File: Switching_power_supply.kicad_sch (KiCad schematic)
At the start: 32 parts, among them J8 Conn_01x03_Pin, SW1 SW_DIP_x04, U4 AMS1117, U5 LM2596HVS-ADJRG

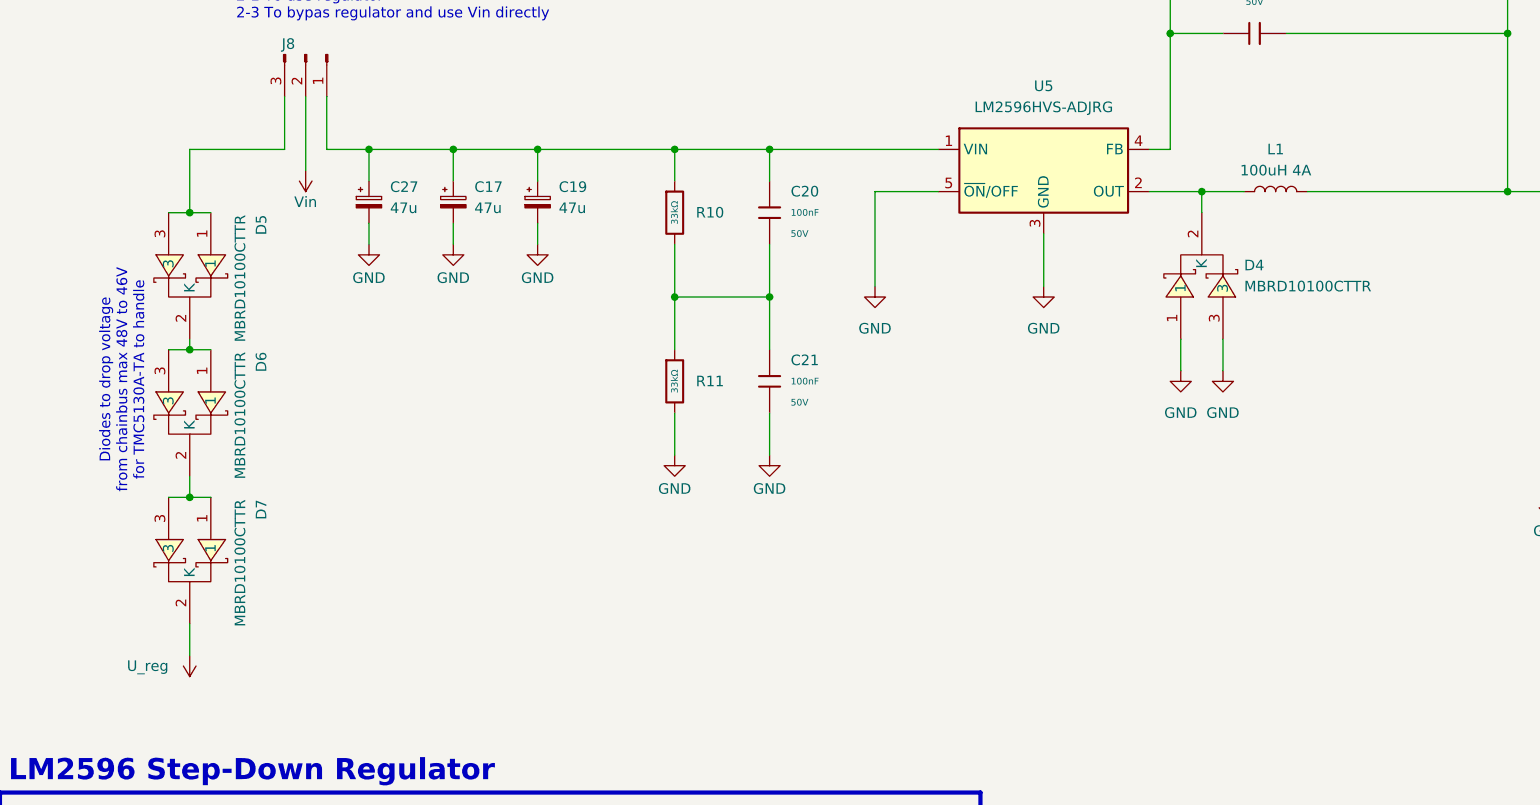
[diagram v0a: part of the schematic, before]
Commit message: added clearance for mounting
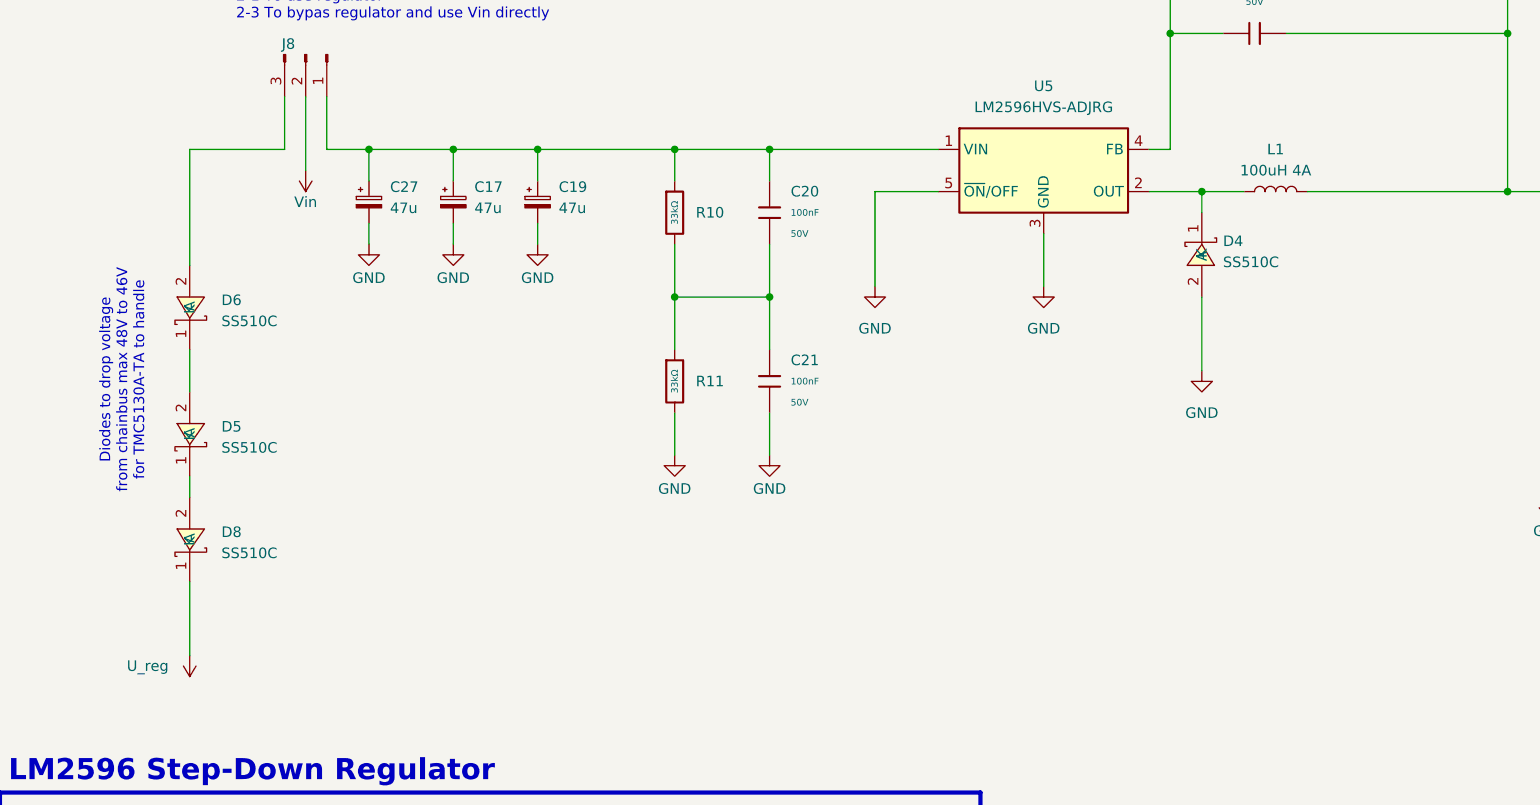
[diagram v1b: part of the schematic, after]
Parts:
- removed D4, D5, D6, D7: MBRD10100CTTR, SMC_MBRD10100CTTR:TO-252-3_L6.5-W5.8-P4.58-TL, symbol SMC_MBRD10100CTTR:MBRD10100CTTR
- added D4, D5, D6, D8: SS510C, SS510C:SMC_L7.1-W6.2-LS8.1-RD, symbol SS510C:SS510C
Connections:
- net GND: now also D4.2 (A)
- net U_reg: now also D8.1 (K)
- net at L1.1, U5.2 (OUT): now also D4.1 (K)
- net at J8.3 (Pin_3): now also D6.2 (A)
- new net: D5.2 (A), D6.1 (K)
- new net: D5.1 (K), D8.2 (A)

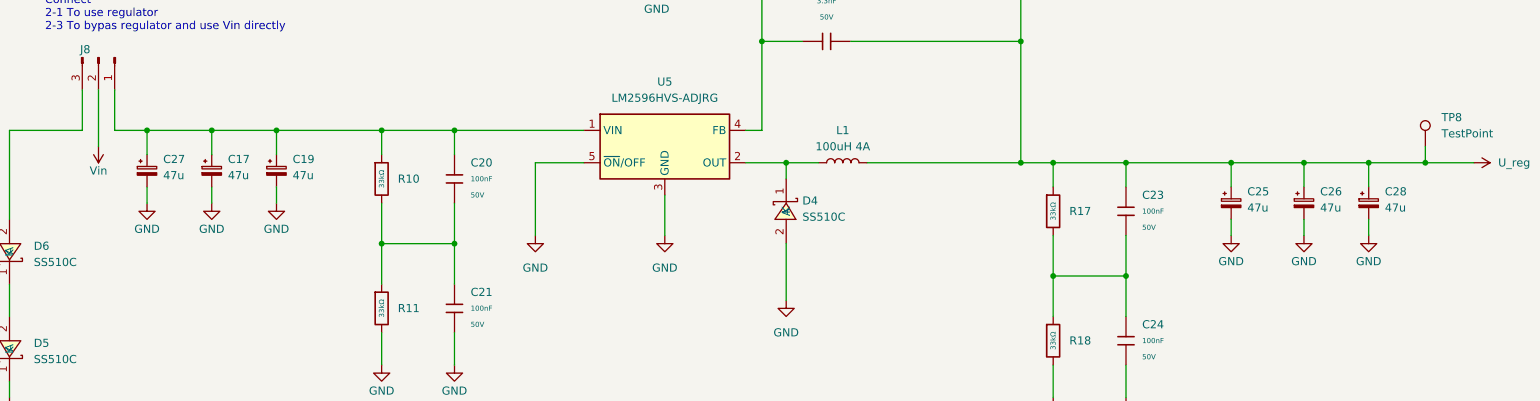
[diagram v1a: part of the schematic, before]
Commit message: moved the converter, to the long side this time
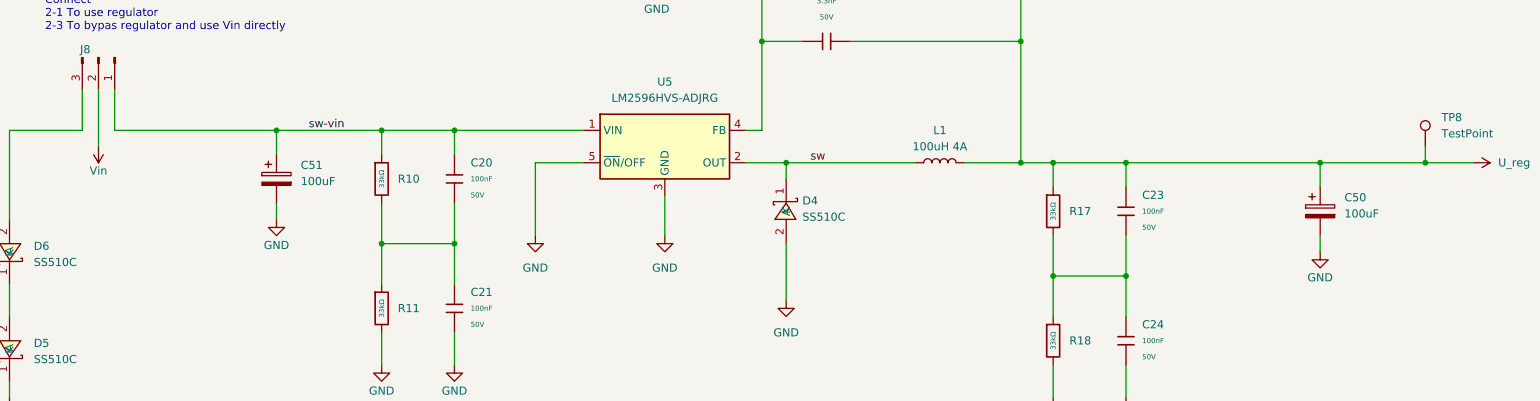
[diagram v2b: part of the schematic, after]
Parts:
- removed C17, C19, C25, C26, C27, C28: 47u, Capacitor_SMD:CP_Elec_6.3x7.7, symbol Device:C_Polarized_Small
- added C50, C51: 100uF, Capacitor_SMD:CP_Elec_10x10, symbol Device:C_Polarized
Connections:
- net GND: now also C50.2, C51.2
- net U_reg: now also C50.1
- net sw-vin: now reaches C20.1, J8.1 (Pin_1), R10.1, U5.1 (VIN)
- net sw-vin: now also C51.1
- net sw: now reaches D4.1 (K), L1.1, U5.2 (OUT)
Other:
- moved on the sheet: L1
